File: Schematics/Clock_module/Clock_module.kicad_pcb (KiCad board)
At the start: 2 copper layers, 101.6 x 78.7 mm, 45 parts, among them J1 Conn_01x06_Female, J2 Power Input, SW1 Mode, SW2 Step, U1 NE555, U2 NE555, U3 NE555, U4 74LS04, U5 74LS32, U6 74LS08

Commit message: PCB RC6
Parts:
- added C9: 1uF, Capacitor_THT:CP_Radial_D5.0mm_P2.50mm, F.Cu at (245.1, 72.4)
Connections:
- R3 pad 2: ~BRK -> Net-(C9-Pad1)
- U2 pad 4: ~BRK -> Net-(C9-Pad1)
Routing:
- net Net-(C9-Pad1): track 0.00 -> 83.4 mm
- net ~BRK: track 96.2 -> 35.8 mm
- net ~CLK: track 36.2 -> 39.5 mm
- net Net-(U5-Pad3): track 38.4 -> 36.1 mm
- net CLK: track 92.9 -> 92.3 mm, vias 2 -> 1

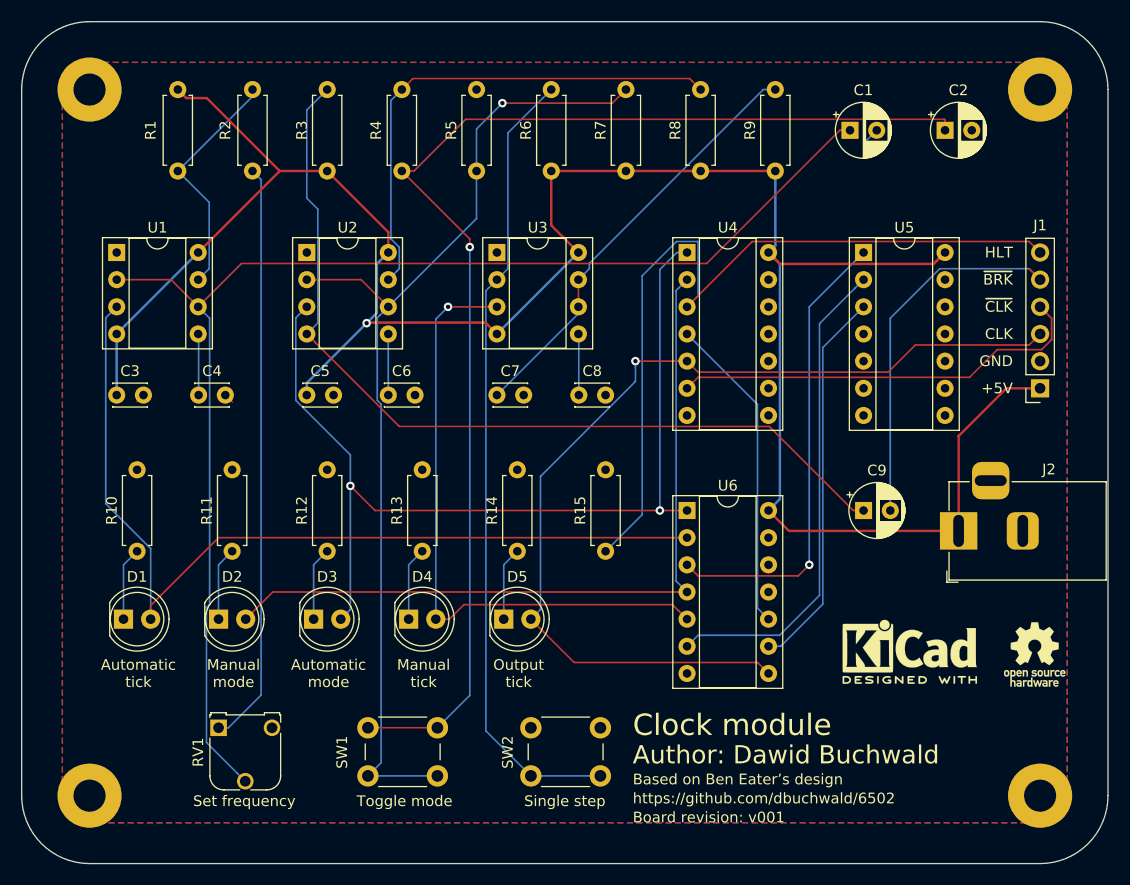
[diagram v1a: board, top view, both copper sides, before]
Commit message: PCB RC9 - replaced potentiometers
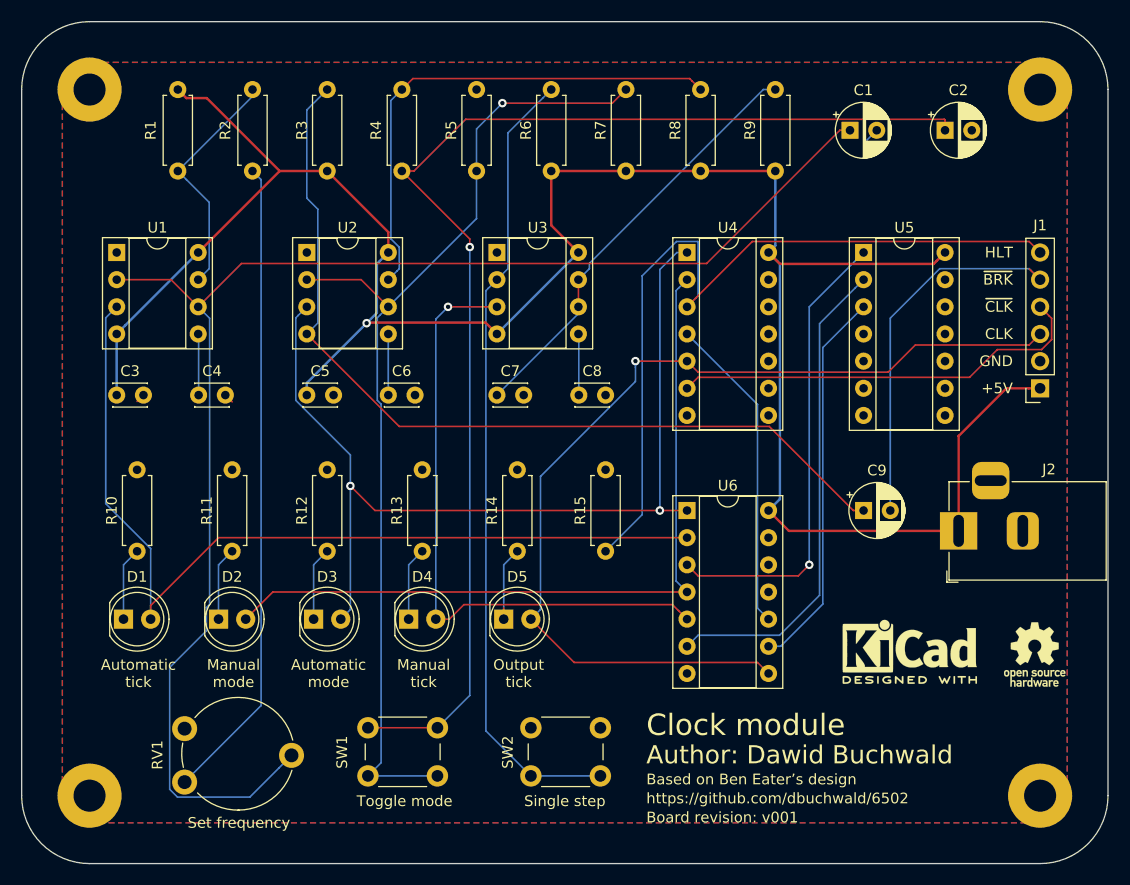
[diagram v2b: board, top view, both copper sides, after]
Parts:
- RV1: value Freq -> 1M; footprint Potentiometer_THT:Potentiometer_Runtron_RM-065_Vertical -> Potentiometer_THT:Potentiometer_Piher_PT-10-V10_Vertical
- moved RV1 5.99 mm to (181.6, 97.8)
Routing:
- net Net-(C1-Pad1): track 122.9 -> 136.9 mm
- net Net-(R2-Pad2): track 54.6 -> 60.4 mm

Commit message: Updated schematic to match changes to BOM
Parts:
- C7: value 330nF -> 0.1uF
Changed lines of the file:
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@@
-(kicad_pcb (version 20171130) (host pcbnew "(5.1.5-0-10_14)")
+(kicad_pcb (version 20171130) (host pcbnew "(5.1.5)-3")
   (general
     (thickness 1.6)
@@
       (effects (font (size 1 1) (thickness 0.15)))
     )
-    (fp_text value 330nF (at 1.25 2.25) (layer F.Fab)
-      (effects (font (size 1 1) (thickness 0.15)))
-    )
+    (fp_text value 0.1uF (at 1.25 2.25) (layer F.Fab)
+      (effects (font (size 1 1) (thickness 0.15)))
+    )
